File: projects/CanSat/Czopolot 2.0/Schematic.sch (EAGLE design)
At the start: 96 parts

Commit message: Schrinking...
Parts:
- removed R10, R11, R12, R13, R14, R6, R7, R8, R9: 10k, Unified:RESISTOR0603
- added D10: LED0805, Unified:LED0805
- added R30: 560R, Unified:RESISTOR0603
- added RN1, RN2: 10k, resistor-dil:4R-NEXBS8V
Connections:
- removed net MPU_FSC: R13.1, U$9.FSYNC
- removed net N$21: C17.2, D1.P$2, U$10.VAC, U$10.VBUS
- new net N$51: D10.P$1, R30.2
- net BMP_SCL: now also RN2A.2, U$1STM32F405RGT6_GPIO.PB6; no longer R6.1, U$1STM32F405RGT6_GPIO.PB10
- net BMP_SDA: now also RN2B.2, U$1STM32F405RGT6_GPIO.PB7; no longer R7.1, U$1STM32F405RGT6_GPIO.PB11
- net BMP_SDI: now also RN2C.2; no longer R8.1
- net BMP_SDO: now also RN2D.2; no longer R9.2
- net GND: now also D10.P$2, RN2D.1, U$9.FSYNC; no longer R9.1
- net LR_BUSY: now also U$1STM32F405RGT6_GPIO.PC5; no longer U$1STM32F405RGT6_GPIO.PC6
- net LR_DIO1: now also U$1STM32F405RGT6_GPIO.PB0; no longer U$1STM32F405RGT6_GPIO.PB2
- net LR_MISO: now also U$1STM32F405RGT6_GPIO.PA6; no longer U$1STM32F405RGT6_GPIO.PB14
- net LR_MOSI: now also U$1STM32F405RGT6_GPIO.PA7; no longer U$1STM32F405RGT6_GPIO.PB15
- net LR_NRST: now also U$1STM32F405RGT6_GPIO.PC4; no longer U$1STM32F405RGT6_GPIO.PC7
- net LR_NSS: now also U$1STM32F405RGT6_GPIO.PA4; no longer U$1STM32F405RGT6_GPIO.PB12
- net LR_SCK: now also U$1STM32F405RGT6_GPIO.PA5; no longer U$1STM32F405RGT6_GPIO.PB13
- net MPU_AD0: now also RN1D.2; no longer R14.1
- net MPU_INT: now also U$1STM32F405RGT6_GPIO.PB2; no longer U$1STM32F405RGT6_GPIO.PB5
- net MPU_NCS: now also RN1C.2; no longer R12.1
- net MPU_SCL: now also RN1B.2, U$1STM32F405RGT6_GPIO.PB10; no longer R11.1, U$1STM32F405RGT6_GPIO.PB6
- net MPU_SDA: now also RN1A.2, U$1STM32F405RGT6_GPIO.PB11; no longer R10.1, U$1STM32F405RGT6_GPIO.PB7
- net USB_VBUS: now also C17.2, D1.P$2, U$10.VAC, U$10.VBUS
- net VCC: now also R30.1, RN1A.1, RN1B.1, RN1C.1, RN1D.1, RN2A.1, RN2B.1, RN2C.1; no longer R10.2, R11.2, R12.2, R13.2, R14.2, R6.2, R7.2, R8.2
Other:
- moved on the sheet: D9, R29

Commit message: Oh God that's small..
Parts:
- removed R26, R27, R28, R29: 560R, Unified:RESISTOR0603
- removed RN1, RN2: 10k, resistor-dil:4R-NEXBS8V
- added R10, R11, R12, R13, R6, R7, R8, R9: 10k, Unified:RESISTOR0603
- added RN3: 560R, resistor-dil:4R-NEXBS8V
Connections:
- net BMP_SCL: now also R6.1; no longer RN2A.2
- net BMP_SDA: now also R7.1; no longer RN2B.2
- net BMP_SDI: now also R8.1; no longer RN2C.2
- net BMP_SDO: now also R9.2; no longer RN2D.2
- net GND: now also R9.1; no longer RN2D.1
- net LR_BUSY: now also U$1STM32F405RGT6_GPIO.PB8; no longer U$1STM32F405RGT6_GPIO.PC5
- net LR_DIO1: now also U$1STM32F405RGT6_GPIO.PB5; no longer U$1STM32F405RGT6_GPIO.PB0
- net LR_NRST: now also U$1STM32F405RGT6_GPIO.PB9; no longer U$1STM32F405RGT6_GPIO.PC4
- net MPU_AD0: now also R10.1; no longer RN1D.2
- net MPU_INT: now also U$1STM32F405RGT6_GPIO.PC7; no longer U$1STM32F405RGT6_GPIO.PB2
- net MPU_NCS: now also R13.1; no longer RN1C.2
- net MPU_SCL: now also R12.1; no longer RN1B.2
- net MPU_SDA: now also R11.1; no longer RN1A.2
- net N$22: no longer U$10.SYS
- net N$43: now also RN3A.1; no longer R26.2
- net N$44: now also RN3B.1; no longer R27.2
- net N$45: now also RN3C.1; no longer R28.2
- net N$46: now also RN3B.2; no longer R27.1
- net N$47: now also RN3A.2; no longer R26.1
- net N$48: now also RN3C.2; no longer R28.1
- net N$49: now also RN3D.1; no longer R29.1
- net N$50: now also RN3D.2; no longer R29.2
- net VCC: now also R10.2, R11.2, R12.2, R13.2, R6.2, R7.2, R8.2; no longer RN1A.1, RN1B.1, RN1C.1, RN1D.1, RN2A.1, RN2B.1, RN2C.1
- net VIN: now also U$10.SYS
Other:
- moved on the sheet: L2

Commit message: Work work..
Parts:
- B2, B3: device SobieskiSat2:BATTERY18650 -> SobieskiSat2:BATTERYPAD
- C14, C15: value 2.2p -> 4p
- U$5: value 12MHz -> 32.768kHz; device SobieskiSat2:OSCILLATOR -> SobieskiSat2:OSCILLATOR_2PIN32X15
- U$6: value 32.768KHz -> 12MHz; device SobieskiSat2:OSCILLATOR -> SobieskiSat2:OSCILLATOR_4PIN32X25
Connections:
- net GND: now also BTN_RST.P$4; no longer BTN_RST.P$1, U$5.GND@1, U$5.GND@2
- net N$11: now also U$6.P$1; no longer U$5.P$1
- net N$12: now also U$6.P$2; no longer U$5.P$2
- net N$13: now also U$5.P$1; no longer U$6.P$1
- net N$14: now also U$5.P$2; no longer U$6.P$2
- net N$16: now also BTN_USR.P$4; no longer BTN_USR.P$1
- net VCC: now also BTN_DFU.P$4; no longer BTN_DFU.P$1
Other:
- moved on the sheet: C11, R2

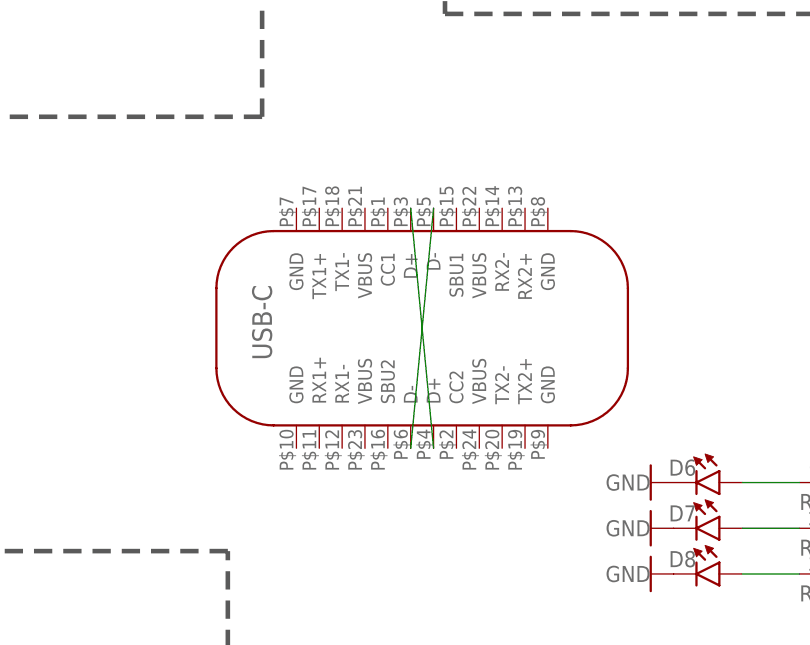
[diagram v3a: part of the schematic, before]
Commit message: USB-C update
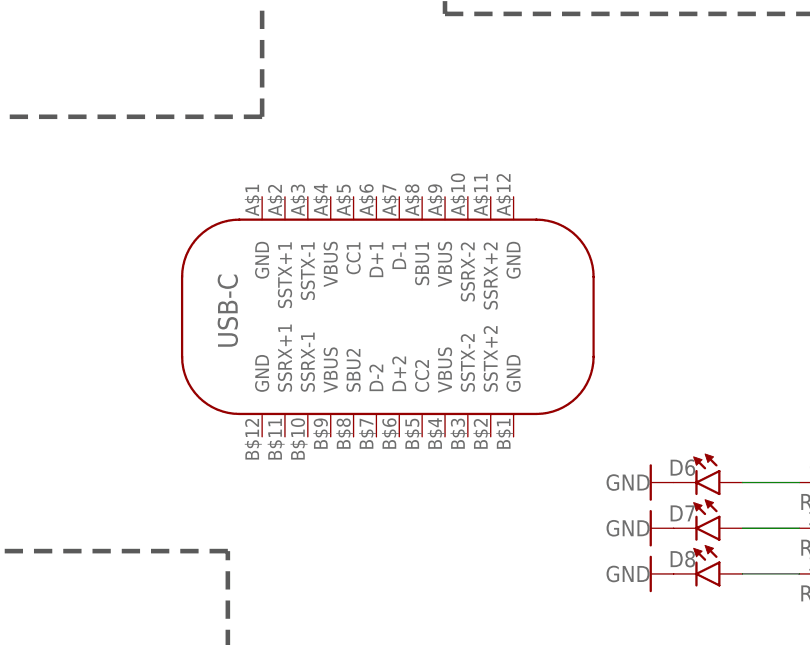
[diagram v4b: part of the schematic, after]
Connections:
- removed net N$41: U$7.D+, U$7.D+@1
- removed net N$42: U$7.D-, U$7.D-@1
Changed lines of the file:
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@@
 <setting verticaltext="up"/>
 </settings>
-<grid distance="0.05" unitdist="inch" unit="inch" style="lines" multiple="1" display="no" altdistance="0.01" altunitdist="inch" altunit="inch"/>
+<grid distance="0.1" unitdist="inch" unit="inch" style="lines" multiple="1" display="no" altdistance="0.01" altunitdist="inch" altunit="inch"/>
 <layers>
 <layer number="1" name="Top" color="4" fill="1" visible="no" active="no"/>
@@
 <part name="C15" library="Unified" deviceset="CAPACITOR" device="0603" package3d_urn="urn:adsk.eagle:package:23616/2" value="4p"/>
 <part name="GND11" library="supply1" library_urn="urn:adsk.eagle:library:371" deviceset="GND" device=""/>
-<part name="U$7" library="SobieskiSat2" deviceset="USB-C" device=""/>
 <part name="R4" library="Unified" deviceset="RESISTOR" device="0603" package3d_urn="urn:adsk.eagle:package:23555/3" value="4.7k"/>
 <part name="GND12" library="supply1" library_urn="urn:adsk.eagle:library:371" deviceset="GND" device=""/>
@@
 <part name="U$5" library="SobieskiSat2" deviceset="OSCILLATOR_2PIN" device="32X15" value="32.768kHz"/>
 <part name="U$6" library="SobieskiSat2" deviceset="OSCILLATOR_4PIN" device="32X25" package3d_urn="urn:adsk.eagle:package:15725817/1" value="12MHz"/>
+<part name="U$7" library="SobieskiSat2" deviceset="USB-C" device=""/>
 </parts>
 <sheets>
@@
 <attribute name="VALUE" x="48.26" y="31.75" size="1.778" layer="96" rot="R270" align="center"/>
 </instance>
-<instance part="U$7" gate="G$1" x="-69.85" y="-11.43" smashed="yes"/>
 <instance part="R4" gate="R$1" x="54.61" y="-16.51" smashed="yes" rot="R90">
 <attribute name="NAME" x="51.435" y="-14.605" size="1.778" layer="95" rot="R180"/>
@@
 <attribute name="VALUE" x="-10.16" y="55.88" size="1.27" layer="96" align="center"/>
 </instance>
+<instance part="U$7" gate="G$1" x="-73.66" y="-10.16" smashed="yes"/>
 </instances>
 <busses>
@@
 </segment>
 </net>
-<net name="N$41" class="0">
-<segment>
-<pinref part="U$7" gate="G$1" pin="D+"/>
-<pinref part="U$7" gate="G$1" pin="D+@1"/>
-<wire x1="-71.12" y1="1.27" x2="-68.58" y2="-25.4" width="0.1524" layer="91"/>
-</segment>
-</net>
-<net name="N$42" class="0">
-<segment>
-<pinref part="U$7" gate="G$1" pin="D-"/>
-<pinref part="U$7" gate="G$1" pin="D-@1"/>
-<wire x1="-68.58" y1="1.27" x2="-71.12" y2="-25.4" width="0.1524" layer="91"/>
-</segment>
-</net>

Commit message: Merge test
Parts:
- U$9: value MPU9250 -> MPU9250USR; device SobieskiSat2:MPU9250 -> SobieskiSat2:MPU9250USR
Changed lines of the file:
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@@
 <part name="C20" library="Unified" deviceset="CAPACITOR" device="0603" package3d_urn="urn:adsk.eagle:package:23616/2" value="1u"/>
 <part name="P+11" library="supply1" library_urn="urn:adsk.eagle:library:371" deviceset="VCC" device=""/>
-<part name="U$9" library="SobieskiSat2" deviceset="MPU9250" device="" package3d_urn="urn:adsk.eagle:package:15487640/1"/>
+<part name="U$9" library="SobieskiSat2" deviceset="MPU9250" device="USR" value="MPU9250USR"/>
 <part name="P+12" library="supply1" library_urn="urn:adsk.eagle:library:371" deviceset="VCC" device=""/>
 <part name="C21" library="Unified" deviceset="CAPACITOR" device="0603" package3d_urn="urn:adsk.eagle:package:23616/2" value="100n"/>

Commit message: Jeezz it's tiny...
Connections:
- net N$10: now also BTN_DFU.P$3; no longer BTN_DFU.P$2
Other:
- moved on the sheet: D4, D5
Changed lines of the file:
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@@
 <attribute name="VALUE" x="-3.81" y="71.12" size="1.778" layer="96" rot="R180"/>
 </instance>
-<instance part="U$12" gate="G$1" x="101.6" y="-53.34" smashed="yes"/>
-<instance part="U$13" gate="G$1" x="132.08" y="-53.34" smashed="yes"/>
-<instance part="GND25" gate="1" x="101.6" y="-66.04" smashed="yes">
-<attribute name="VALUE" x="101.6" y="-67.31" size="1.778" layer="96" align="center"/>
-</instance>
-<instance part="GND26" gate="1" x="132.08" y="-66.04" smashed="yes">
-<attribute name="VALUE" x="132.08" y="-67.31" size="1.778" layer="96" align="center"/>
-</instance>
-<instance part="D4" gate="G$1" x="109.22" y="-53.34" smashed="yes">
-<attribute name="NAME" x="110.49" y="-52.07" size="1.778" layer="95"/>
-</instance>
-<instance part="D5" gate="G$1" x="139.7" y="-53.34" smashed="yes">
-<attribute name="NAME" x="140.97" y="-52.07" size="1.778" layer="95"/>
+<instance part="U$12" gate="G$1" x="99.06" y="-71.12" smashed="yes"/>
+<instance part="U$13" gate="G$1" x="129.54" y="-71.12" smashed="yes"/>
+<instance part="GND25" gate="1" x="99.06" y="-83.82" smashed="yes">
+<attribute name="VALUE" x="99.06" y="-85.09" size="1.778" layer="96" align="center"/>
+</instance>
+<instance part="GND26" gate="1" x="129.54" y="-83.82" smashed="yes">
+<attribute name="VALUE" x="129.54" y="-85.09" size="1.778" layer="96" align="center"/>
+</instance>
+<instance part="D4" gate="G$1" x="106.68" y="-71.12" smashed="yes">
+<attribute name="NAME" x="107.95" y="-69.85" size="1.778" layer="95"/>
+</instance>
+<instance part="D5" gate="G$1" x="137.16" y="-71.12" smashed="yes">
+<attribute name="NAME" x="138.43" y="-69.85" size="1.778" layer="95"/>
 </instance>
 <instance part="C32" gate="C$1" x="-44.45" y="72.39" smashed="yes" rot="R90">
@@
 <pinref part="GND25" gate="1" pin="GND"/>
 <pinref part="U$12" gate="G$1" pin="P$1"/>
-<wire x1="101.6" y1="-63.5" x2="101.6" y2="-62.23" width="0.1524" layer="91"/>
+<wire x1="99.06" y1="-81.28" x2="99.06" y2="-80.01" width="0.1524" layer="91"/>
 <pinref part="D4" gate="G$1" pin="P$1"/>
-<wire x1="101.6" y1="-62.23" x2="101.6" y2="-59.69" width="0.1524" layer="91"/>
-<wire x1="101.6" y1="-62.23" x2="109.22" y2="-62.23" width="0.1524" layer="91"/>
-<wire x1="109.22" y1="-62.23" x2="109.22" y2="-57.15" width="0.1524" layer="91"/>
-<junction x="101.6" y="-62.23"/>
+<wire x1="99.06" y1="-80.01" x2="99.06" y2="-77.47" width="0.1524" layer="91"/>
+<wire x1="99.06" y1="-80.01" x2="106.68" y2="-80.01" width="0.1524" layer="91"/>
+<wire x1="106.68" y1="-80.01" x2="106.68" y2="-74.93" width="0.1524" layer="91"/>
+<junction x="99.06" y="-80.01"/>
 </segment>
 <segment>
 <pinref part="U$13" gate="G$1" pin="P$1"/>
 <pinref part="GND26" gate="1" pin="GND"/>
-<wire x1="132.08" y1="-59.69" x2="132.08" y2="-62.23" width="0.1524" layer="91"/>
+<wire x1="129.54" y1="-77.47" x2="129.54" y2="-80.01" width="0.1524" layer="91"/>
 <pinref part="D5" gate="G$1" pin="P$1"/>
-<wire x1="132.08" y1="-62.23" x2="132.08" y2="-63.5" width="0.1524" layer="91"/>
-<wire x1="132.08" y1="-62.23" x2="139.7" y2="-62.23" width="0.1524" layer="91"/>
-<wire x1="139.7" y1="-62.23" x2="139.7" y2="-57.15" width="0.1524" layer="91"/>
-<junction x="132.08" y="-62.23"/>
+<wire x1="129.54" y1="-80.01" x2="129.54" y2="-81.28" width="0.1524" layer="91"/>
+<wire x1="129.54" y1="-80.01" x2="137.16" y2="-80.01" width="0.1524" layer="91"/>
+<wire x1="137.16" y1="-80.01" x2="137.16" y2="-74.93" width="0.1524" layer="91"/>
+<junction x="129.54" y="-80.01"/>
 </segment>
 <segment>
@@
 <pinref part="U$1" gate="STM32F405RGT6_UTL" pin="BOOT0"/>
 <wire x1="-34.29" y1="67.31" x2="2.54" y2="67.31" width="0.1524" layer="91"/>
-<wire x1="-34.29" y1="67.31" x2="-34.29" y2="69.85" width="0.1524" layer="91"/>
 <pinref part="C32" gate="C$1" pin="2"/>
-<wire x1="-34.29" y1="69.85" x2="-34.29" y2="72.39" width="0.1524" layer="91"/>
+<wire x1="-34.29" y1="67.31" x2="-34.29" y2="72.39" width="0.1524" layer="91"/>
 <wire x1="-34.29" y1="72.39" x2="-34.29" y2="77.47" width="0.1524" layer="91"/>
 <wire x1="-39.37" y1="72.39" x2="-34.29" y2="72.39" width="0.1524" layer="91"/>
 <junction x="-34.29" y="72.39"/>
-<pinref part="BTN_DFU" gate="G$1" pin="P$2"/>
-<wire x1="-35.56" y1="69.85" x2="-34.29" y2="69.85" width="0.1524" layer="91"/>
-<junction x="-34.29" y="69.85"/>
+<pinref part="BTN_DFU" gate="G$1" pin="P$3"/>
+<wire x1="-35.56" y1="64.77" x2="-35.56" y2="67.31" width="0.1524" layer="91"/>
+<wire x1="-35.56" y1="67.31" x2="-34.29" y2="67.31" width="0.1524" layer="91"/>
+<junction x="-34.29" y="67.31"/>
 </segment>
 </net>
@@
 <segment>
 <pinref part="U$12" gate="G$1" pin="P$2"/>
-<wire x1="101.6" y1="-46.99" x2="101.6" y2="-45.72" width="0.1524" layer="91"/>
+<wire x1="99.06" y1="-64.77" x2="99.06" y2="-63.5" width="0.1524" layer="91"/>
 <pinref part="D4" gate="G$1" pin="P$2"/>
-<wire x1="101.6" y1="-45.72" x2="109.22" y2="-45.72" width="0.1524" layer="91"/>
-<wire x1="109.22" y1="-45.72" x2="109.22" y2="-49.53" width="0.1524" layer="91"/>
+<wire x1="99.06" y1="-63.5" x2="106.68" y2="-63.5" width="0.1524" layer="91"/>
+<wire x1="106.68" y1="-63.5" x2="106.68" y2="-67.31" width="0.1524" layer="91"/>
 </segment>
 </net>
@@
 <segment>
 <pinref part="U$13" gate="G$1" pin="P$2"/>
-<wire x1="132.08" y1="-46.99" x2="132.08" y2="-45.72" width="0.1524" layer="91"/>
+<wire x1="129.54" y1="-64.77" x2="129.54" y2="-63.5" width="0.1524" layer="91"/>
 <pinref part="D5" gate="G$1" pin="P$2"/>
-<wire x1="132.08" y1="-45.72" x2="139.7" y2="-45.72" width="0.1524" layer="91"/>
-<wire x1="139.7" y1="-45.72" x2="139.7" y2="-49.53" width="0.1524" layer="91"/>
-</segment>
-</net>
+<wire x1="129.54" y1="-63.5" x2="137.16" y2="-63.5" width="0.1524" layer="91"/>
+<wire x1="137.16" y1="-63.5" x2="137.16" y2="-67.31" width="0.1524" layer="91"/>
+</segment>
+</net>

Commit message: Work work...
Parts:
- added R14: 7k, Unified:RESISTOR0603
- added R26: 11k, Unified:RESISTOR0603
- added R27: 12k, Unified:RESISTOR0603
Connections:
- new net N$21: R26.1, R27.2
- net B+: now also R14.2
- net GND: now also BTN_RST.P$1, BTN_USR.P$1, R27.1; no longer BTN_RST.P$4, BTN_USR.P$2, R19.2
- net GPS_RX: now also U$1STM32F405RGT6_GPIO.PC6, U$3.RX; no longer D61.P$2, U$1STM32F405RGT6_GPIO.PA2
- net GPS_TX: now also U$1STM32F405RGT6_GPIO.PC7; no longer U$1STM32F405RGT6_GPIO.PA3
- net MPU_INT: now also U$1STM32F405RGT6_GPIO.PB15; no longer U$1STM32F405RGT6_GPIO.PC7
- net N$10: now also BTN_DFU.P$2; no longer BTN_DFU.P$3
- net N$16: now also BTN_USR.P$2; no longer BTN_USR.P$4
- net N$18: now also R14.1, R26.2; no longer D61.P$1, R63.1, U$3.RX
- net N$29: no longer R19.1
- net VCC: now also BTN_DFU.P$1; no longer BTN_DFU.P$4, R63.2
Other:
- moved on the sheet: D61, R19, R63

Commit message: Work work
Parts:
- removed RN3: 560R, resistor-dil:4R-NEXBS8V
- added R28, R29: ?10k, Unified:RESISTOR0603
- added R31, R33: 100k, Unified:RESISTOR0603
- added RN1: (no value), resistor-dil:4R-NEXBV8V
- added U$14, U$15: NMOSFET, SobieskiSat2:NMOSFET
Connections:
- net N$4 renamed SD_CLK
- removed net N$39: D4.P$2, U$12.P$2
- removed net N$40: D5.P$2, U$13.P$2
- removed net N$46: RN3B.2, U$1STM32F405RGT6_GPIO.PA14
- removed net N$47: RN3A.2, U$1STM32F405RGT6_GPIO.PA13
- removed net N$48: RN3C.2, U$1STM32F405RGT6_GPIO.PA15
- removed net N$5: U$1STM32F405RGT6_UTL.PD2, U$2.DAT0
- removed net N$6: R1.2, U$1STM32F405RGT6_UTL.PC11, U$2.DAT1
- new net IN_MOT1: R28.2, U$14.G
- new net IN_MOT2: R29.2, U$15.G
- new net N$41: D5.P$1, U$13.P$1, U$15.D
- new net N$42: D4.P$1, U$12.P$1, U$14.D
- new net SD_CMD: U$1STM32F405RGT6_UTL.PD2, U$2.CMD
- new net SD_D0: U$1STM32F405RGT6_UTL.PC8, U$2.DAT0
- new net SD_D1: U$1STM32F405RGT6_UTL.PC9, U$2.DAT1
- new net SD_D2: U$1STM32F405RGT6_UTL.PC10, U$2.DAT2
- new net SD_D3: R1.2, U$1STM32F405RGT6_UTL.PC11, U$2.DAT3
- net GND: now also R28.1, R29.1, U$14.S, U$15.S; no longer D4.P$1, D5.P$1, U$12.P$1, U$13.P$1
- net N$1: now also RN1A.2; no longer U$1STM32F405RGT6_UTL.PC8, U$2.CMD
- net N$2: now also RN1C.2; no longer U$1STM32F405RGT6_UTL.PC9, U$2.DAT3
- net N$3: now also RN1B.2; no longer U$1STM32F405RGT6_UTL.PA8, U$2.DAT2
- net N$43: now also RN1A.1; no longer RN3A.1
- net N$44: now also RN1B.1; no longer RN3B.1
- net N$45: now also RN1C.1; no longer RN3C.1
- net N$49: now also RN1D.1; no longer RN3D.1
- net N$50: now also RN1D.2; no longer RN3D.2, U$1STM32F405RGT6_GPIO.PB4
- net SD_SW: now also U$1STM32F405RGT6_UTL.PA8; no longer U$1STM32F405RGT6_UTL.PC10
- net VCC: now also R31.1, R33.1
- net VIN: now also D4.P$2, D5.P$2, U$12.P$2, U$13.P$2
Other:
- moved on the sheet: BTN_USR, D5, D6, D7, D8, D9, R1, R4
